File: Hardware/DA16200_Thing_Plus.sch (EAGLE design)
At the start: 60 parts, among them J1 MICRO-SDFRICTION, J2 THING_PLUS, J3 Qwiic, J5 USB C, J6 microSD, J7 CORTEX_JTAG_DEBUG_PTH_NS, Q1 20V/4.2A/52mΩ/1.4W, U1 DA16200MOD, U2 CH340E_MSOP10, U3 MCP73831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

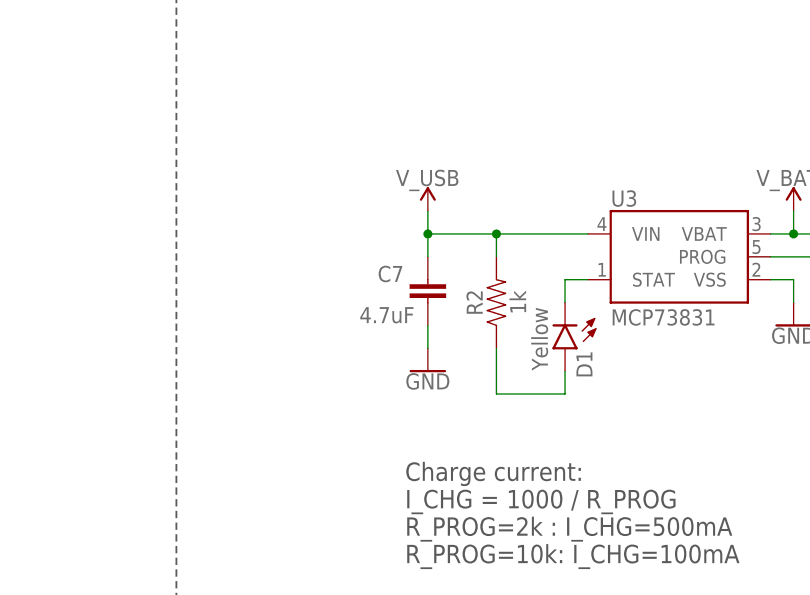
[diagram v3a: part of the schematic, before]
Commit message: Add charge LED jumper
Add charge LED jumper
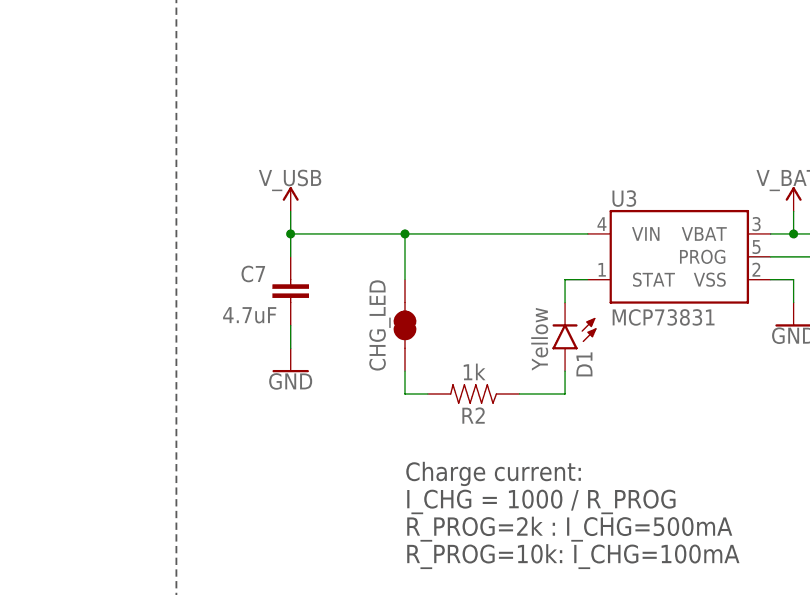
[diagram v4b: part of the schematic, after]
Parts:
- added CHG_LED: JUMPER-SMT_2_NC_TRACE_SILK, SparkFun-Jumpers:JUMPER-SMT_2_NC_TRACE_SILK
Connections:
- new net N$23: CHG_LED.1, R2.2
- net V_USB: now also CHG_LED.2; no longer R2.2
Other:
- moved on the sheet: C7, R2
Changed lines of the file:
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@@
 <part name="S1" library="SparkFun-Switches" deviceset="SWITCH-SPDT" device="-SMD-AYZ0202"/>
 <part name="J1" library="SparkFun-Connectors" deviceset="MICRO-SD" device="FRICTION"/>
+<part name="CHG_LED" library="SparkFun-Jumpers" deviceset="JUMPER-SMT_2_NC_TRACE" device="_SILK" package3d_urn="urn:adsk.eagle:package:39281/1"/>
 </parts>
 <sheets>
@@
 <attribute name="VALUE" x="91.44" y="220.726" size="1.778" layer="96" align="top-center"/>
 </instance>
-<instance part="GND4" gate="1" x="149.86" y="228.6" smashed="yes">
-<attribute name="VALUE" x="149.86" y="228.346" size="1.778" layer="96" align="top-center"/>
+<instance part="GND4" gate="1" x="134.62" y="228.6" smashed="yes">
+<attribute name="VALUE" x="134.62" y="228.346" size="1.778" layer="96" align="top-center"/>
 </instance>
 <instance part="GND9" gate="1" x="190.5" y="233.68" smashed="yes">
@@
 <attribute name="VALUE" x="20.32" y="246.634" size="1.778" layer="96" align="bottom-center"/>
 </instance>
-<instance part="SUPPLY22" gate="G$1" x="149.86" y="246.38" smashed="yes">
-<attribute name="VALUE" x="149.86" y="249.174" size="1.778" layer="96" align="bottom-center"/>
+<instance part="SUPPLY22" gate="G$1" x="134.62" y="246.38" smashed="yes">
+<attribute name="VALUE" x="134.62" y="249.174" size="1.778" layer="96" align="bottom-center"/>
 </instance>
 <instance part="SUPPLY23" gate="G$1" x="299.72" y="243.84" smashed="yes">
@@
 <attribute name="VALUE" x="92.964" y="226.441" size="1.778" layer="96" font="vector"/>
 </instance>
-<instance part="R2" gate="G$1" x="157.48" y="236.22" smashed="yes" rot="R90">
-<attribute name="NAME" x="155.956" y="236.22" size="1.778" layer="95" font="vector" rot="R90" align="bottom-center"/>
-<attribute name="VALUE" x="159.004" y="236.22" size="1.778" layer="96" font="vector" rot="R90" align="top-center"/>
+<instance part="R2" gate="G$1" x="154.94" y="226.06" smashed="yes" rot="R180">
+<attribute name="NAME" x="154.94" y="224.536" size="1.778" layer="95" font="vector" rot="R180" align="bottom-center"/>
+<attribute name="VALUE" x="154.94" y="227.584" size="1.778" layer="96" font="vector" rot="R180" align="top-center"/>
 </instance>
 <instance part="R3" gate="G$1" x="312.42" y="86.36" smashed="yes" rot="R90">
@@
 <attribute name="VALUE" x="313.944" y="86.36" size="1.778" layer="96" font="vector" rot="R90" align="top-center"/>
 </instance>
-<instance part="C7" gate="G$1" x="149.86" y="236.22" smashed="yes">
-<attribute name="NAME" x="144.272" y="238.506" size="1.778" layer="95" font="vector"/>
-<attribute name="VALUE" x="142.24" y="233.934" size="1.778" layer="96" font="vector"/>
+<instance part="C7" gate="G$1" x="134.62" y="236.22" smashed="yes">
+<attribute name="NAME" x="129.032" y="238.506" size="1.778" layer="95" font="vector"/>
+<attribute name="VALUE" x="127" y="233.934" size="1.778" layer="96" font="vector"/>
 </instance>
 <instance part="C10" gate="G$1" x="226.06" y="236.22" smashed="yes">
@@
 <attribute name="NAME" x="106.68" y="61.468" size="1.778" layer="95"/>
 <attribute name="VALUE" x="106.68" y="33.02" size="1.778" layer="96"/>
+</instance>
+<instance part="CHG_LED" gate="G$1" x="147.32" y="233.68" smashed="yes" rot="R90">
+<attribute name="NAME" x="144.272" y="233.68" size="1.778" layer="95" font="vector" rot="R90" align="center"/>
 </instance>
 </instances>
@@
 </segment>
 <segment>
-<wire x1="149.86" y1="231.14" x2="149.86" y2="233.68" width="0.1524" layer="91"/>
+<wire x1="134.62" y1="231.14" x2="134.62" y2="233.68" width="0.1524" layer="91"/>
 <pinref part="GND4" gate="1" pin="GND"/>
 <pinref part="C7" gate="G$1" pin="2"/>
@@
 </segment>
 <segment>
-<wire x1="167.64" y1="243.84" x2="157.48" y2="243.84" width="0.1524" layer="91"/>
-<wire x1="157.48" y1="243.84" x2="149.86" y2="243.84" width="0.1524" layer="91"/>
-<wire x1="149.86" y1="243.84" x2="149.86" y2="246.38" width="0.1524" layer="91"/>
-<wire x1="149.86" y1="243.84" x2="149.86" y2="241.3" width="0.1524" layer="91"/>
-<junction x="149.86" y="243.84"/>
-<wire x1="157.48" y1="241.3" x2="157.48" y2="243.84" width="0.1524" layer="91"/>
-<junction x="157.48" y="243.84"/>
+<wire x1="167.64" y1="243.84" x2="147.32" y2="243.84" width="0.1524" layer="91"/>
+<wire x1="147.32" y1="243.84" x2="134.62" y2="243.84" width="0.1524" layer="91"/>
+<wire x1="134.62" y1="243.84" x2="134.62" y2="246.38" width="0.1524" layer="91"/>
+<wire x1="134.62" y1="243.84" x2="134.62" y2="241.3" width="0.1524" layer="91"/>
+<junction x="134.62" y="243.84"/>
 <pinref part="SUPPLY22" gate="G$1" pin="V_USB"/>
 <pinref part="U3" gate="G$1" pin="VIN"/>
-<pinref part="R2" gate="G$1" pin="2"/>
 <pinref part="C7" gate="G$1" pin="1"/>
+<pinref part="CHG_LED" gate="G$1" pin="2"/>
+<wire x1="147.32" y1="238.76" x2="147.32" y2="243.84" width="0.1524" layer="91"/>
+<junction x="147.32" y="243.84"/>
 </segment>
 <segment>
@@
 <net name="N$17" class="0">
 <segment>
-<wire x1="165.1" y1="226.06" x2="157.48" y2="226.06" width="0.1524" layer="91"/>
+<wire x1="165.1" y1="226.06" x2="160.02" y2="226.06" width="0.1524" layer="91"/>
 <pinref part="D1" gate="G$1" pin="A"/>
 <wire x1="165.1" y1="228.6" x2="165.1" y2="226.06" width="0.1524" layer="91"/>
-<wire x1="157.48" y1="226.06" x2="157.48" y2="231.14" width="0.1524" layer="91"/>
 <pinref part="R2" gate="G$1" pin="1"/>
 </segment>
@@
 </segment>
 </net>
+<net name="N$23" class="0">
+<segment>
+<pinref part="R2" gate="G$1" pin="2"/>
+<wire x1="149.86" y1="226.06" x2="147.32" y2="226.06" width="0.1524" layer="91"/>
+<pinref part="CHG_LED" gate="G$1" pin="1"/>
+<wire x1="147.32" y1="226.06" x2="147.32" y2="228.6" width="0.1524" layer="91"/>
+</segment>
+</net>

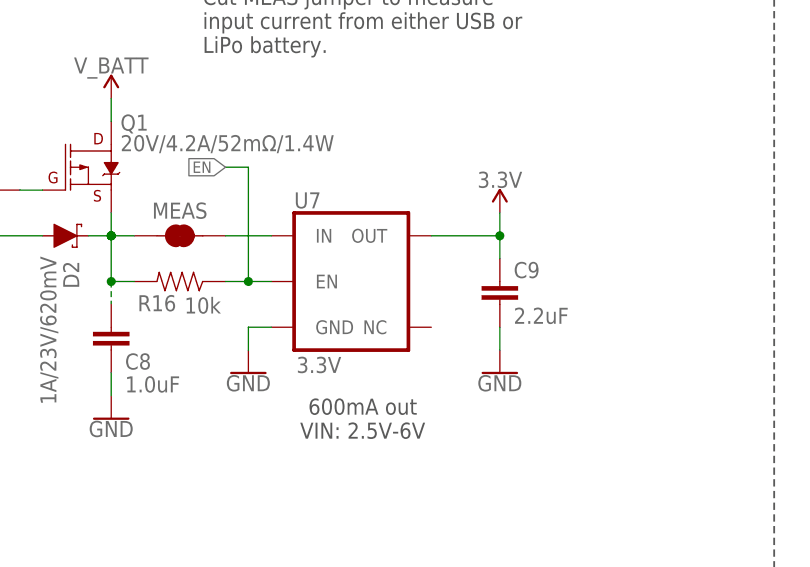
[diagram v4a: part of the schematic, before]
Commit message: Update AP2112K to XC6222B33
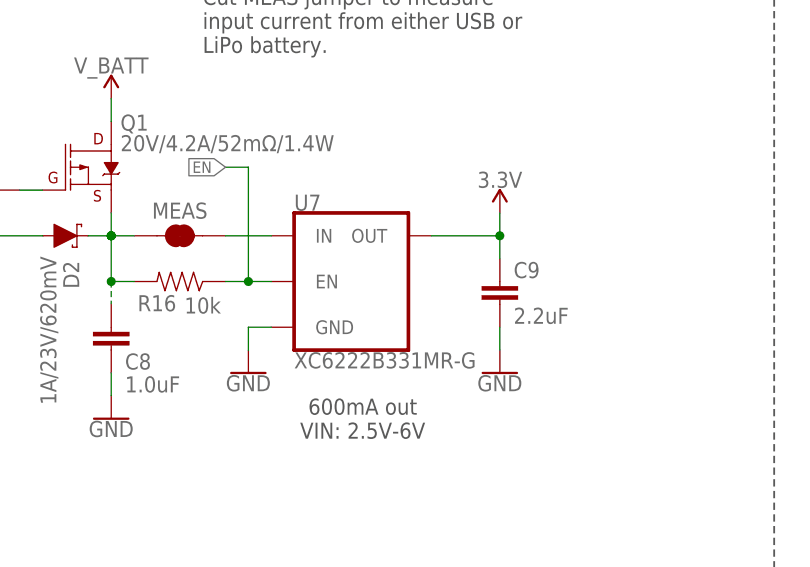
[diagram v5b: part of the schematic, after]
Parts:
- U7: value 3.3V -> XC6222B331MR-G; device SparkFun-IC-Power:V_REG_AP2112K-3.3V -> SparkFun-IC-Power:XC6222B331MR-G
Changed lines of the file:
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@@
 <part name="SUPPLY1" library="SparkFun-PowerSymbols" deviceset="3.3V" device=""/>
 <part name="SUPPLY15" library="SparkFun-PowerSymbols" deviceset="3.3V" device=""/>
-<part name="U7" library="SparkFun-IC-Power" deviceset="V_REG_AP2112" device="K-3.3V" value="3.3V"/>
+<part name="U7" library="SparkFun-IC-Power" deviceset="XC6222" device="B331MR-G" value="XC6222B331MR-G"/>
 <part name="U3" library="SparkFun-IC-Power" deviceset="MCP73831" device=""/>
 <part name="R10" library="SparkFun-Resistors" deviceset="2.2KOHM" device="-0402T-1/16W-1%" value="2.2k"/>
@@
 </instance>
 <instance part="U7" gate="G$1" x="76.2" y="231.14" smashed="yes">
-<attribute name="NAME" x="68.58" y="239.268" size="1.778" layer="95" font="vector"/>
-<attribute name="VALUE" x="68.834" y="220.98" size="1.778" layer="96" font="vector" rot="MR180" align="top-left"/>
+<attribute name="NAME" x="68.58" y="239.014" size="1.778" layer="95" font="vector"/>
+<attribute name="VALUE" x="68.58" y="223.266" size="1.778" layer="96" font="vector" align="top-left"/>
 </instance>
 <instance part="U3" gate="G$1" x="177.8" y="241.3" smashed="yes">
